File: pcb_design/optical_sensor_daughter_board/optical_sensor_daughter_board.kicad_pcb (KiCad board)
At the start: 2 copper layers, 22.9 x 44.5 mm, 2 parts, among them J1 Conn_02x06_Counter_Clockwise, U1 PMW3389

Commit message: WIP daughter board
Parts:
- added C1: 0.1uF, Capacitor_SMD:C_0603_1608Metric_Pad1.05x0.95mm_HandSolder, F.Cu at (137.7, 85.2)
- added C2: 4.7uF, Capacitor_SMD:C_0603_1608Metric_Pad1.05x0.95mm_HandSolder, F.Cu at (139.6, 85.2)
- added C3: 1uF, Capacitor_SMD:C_0603_1608Metric_Pad1.05x0.95mm_HandSolder, F.Cu at (144.3, 110.0)
- added C4: 1uF, Capacitor_SMD:C_0603_1608Metric_Pad1.05x0.95mm_HandSolder, F.Cu at (130.4, 109.2)
- added R1: 10K, Resistor_SMD:R_0603_1608Metric_Pad1.05x0.95mm_HandSolder, F.Cu at (141.3, 85.2)
- added R2: 39, Resistor_SMD:R_0603_1608Metric_Pad1.05x0.95mm_HandSolder, F.Cu at (126.7, 109.2)
- added U2: PMW3360, pmw3389:PMW3389, F.Cu at (135.6, 96.8)
- added U3: SN74LVC1T45DBV, Package_TO_SOT_SMD:SOT-23-6, F.Cu at (126.6, 87.2)
- added U4: SN74LVC1T45DBV, Package_TO_SOT_SMD:SOT-23-6, F.Cu at (126.5, 94.8)
- added U5: SN74LVC1T45DBV, Package_TO_SOT_SMD:SOT-23-6, F.Cu at (126.5, 98.7)
- added U6: SN74LVC1T45DBV, Package_TO_SOT_SMD:SOT-23-6, F.Cu at (126.5, 102.5)
- added U7: SN74LVC1T45DBV, Package_TO_SOT_SMD:SOT-23-6, F.Cu at (126.6, 91.0)
- J1: value Conn_02x06_Counter_Clockwise -> Conn_01x08_Male; footprint Connector_PinHeader_2.54mm:PinHeader_2x06_P2.54mm_Vertical -> Connector_PinHeader_2.54mm:PinHeader_1x08_P2.54mm_Vertical
- U1: value PMW3389 -> TLV70019_SOT23-5; footprint pmw3389:PMW3389 -> Package_TO_SOT_SMD:SOT-23-5
- moved J1 13.7 mm to (143.9, 106.0)
- moved U1 9.62 mm to (140.3, 109.2)
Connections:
- J1 pad 1: GND -> VIN
- J1 pad 2: MOTION -> MISO_3.3V
- J1 pad 3: NRESET -> MOIS_3.3V
- J1 pad 4: SCLK -> SLCK_3.3V
- J1 pad 5: GPO -> SS_3.3V
- J1 pad 6: MOSI -> MOTION_3.3V
- J1 pad 7: VDDIO -> GND
- J1 pad 8: MISO -> RESET
- U1 pad 1: (no net) -> VIN
- U1 pad 2: (no net) -> Net-(C3-Pad2)
- U1 pad 3: VDCPIX -> VIN
- U1 pad 4: VDD -> (no net)
- U1 pad 5: VDDIO -> VDD
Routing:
- net VDD: track 27.5 -> 97.6 mm, vias 0 -> 4
- net VIN: track 0.00 -> 65.4 mm
- net GND: track 9.00 -> 62.9 mm
- net SLCK_3.3V: track 0.00 -> 45.3 mm, vias 0 -> 2
- net MISO_3.3V: track 0.00 -> 37.0 mm, vias 0 -> 1
- net SS_3.3V: track 0.00 -> 36.1 mm, vias 0 -> 3
- net MOIS_3.3V: track 0.00 -> 33.0 mm, vias 0 -> 1
- net LED_P: track 33.0 -> 0.00 mm
- net VDCPIX: track 32.7 -> 0.00 mm
- net MOTION_3.3V: track 0.00 -> 28.2 mm, vias 0 -> 1
- net NCS: track 26.5 -> 0.00 mm
- net Net-(C3-Pad2): track 0.00 -> 23.4 mm
- net VDDIO: track 22.8 -> 0.00 mm
- net GPO: track 18.1 -> 0.00 mm
- net Net-(C1-Pad2): track 0.00 -> 17.9 mm
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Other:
- board size 22.9 x 44.5 mm -> 23 x 28 mm

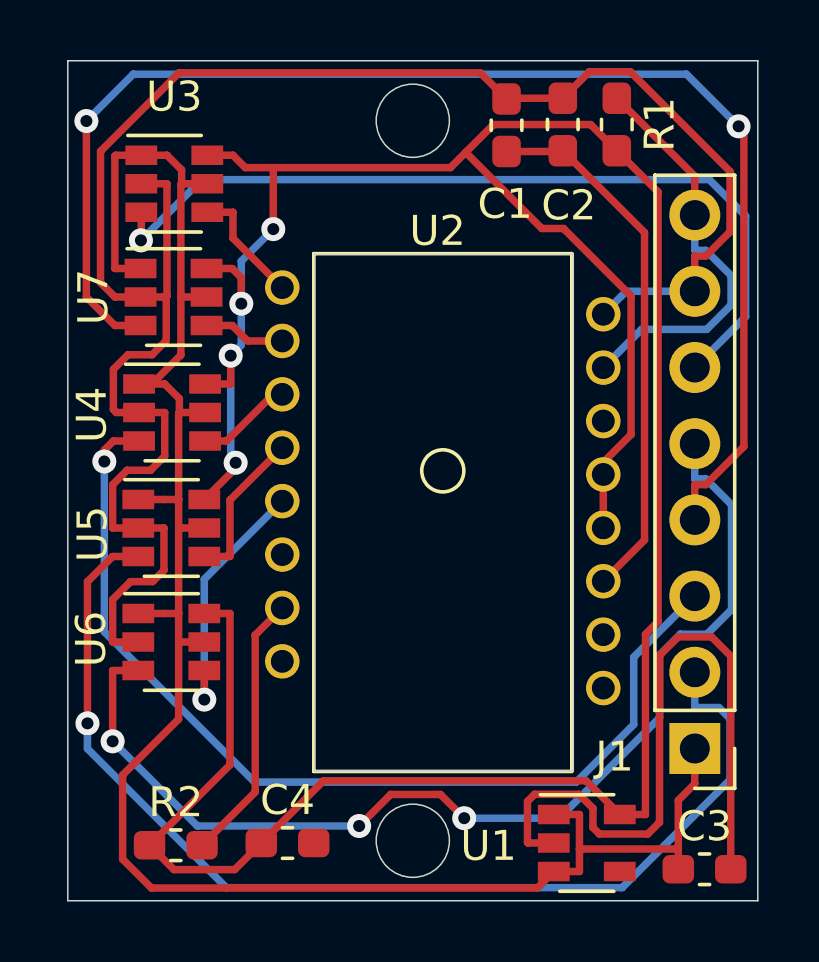
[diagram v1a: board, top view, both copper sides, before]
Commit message: New 0x08 firmware added
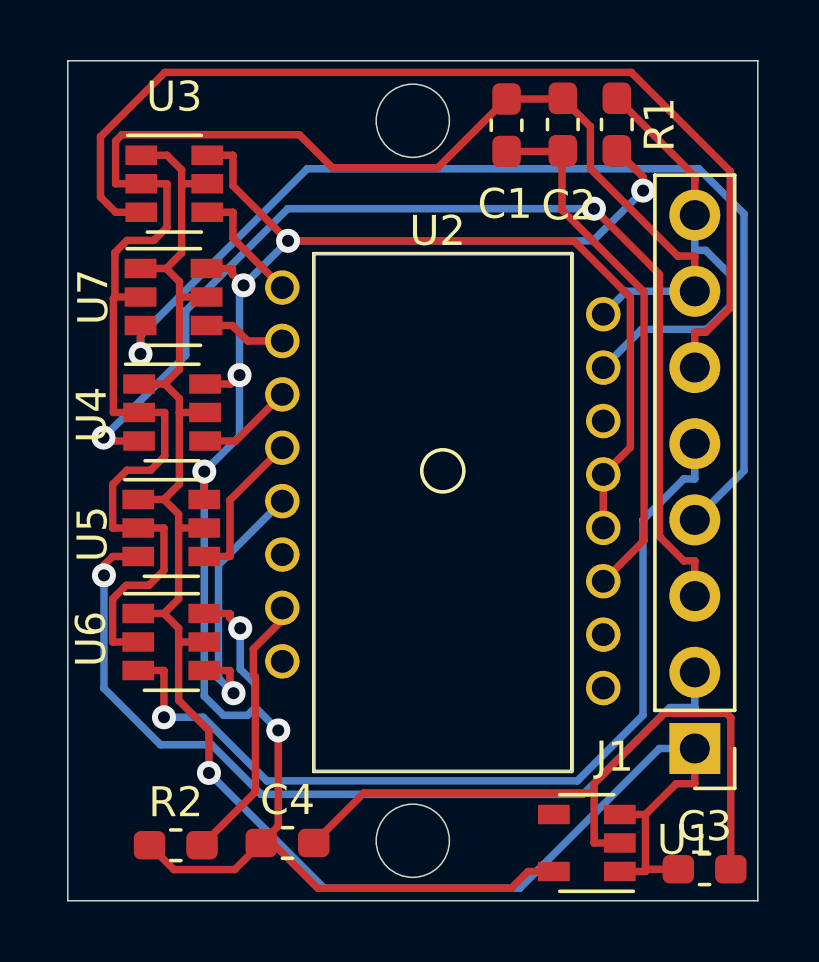
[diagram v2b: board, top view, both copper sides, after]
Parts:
- turned U1 to 180 degrees
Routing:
- net VDD: track 97.6 -> 85.5 mm, vias 4 -> 7
- net SLCK_3.3V: track 45.3 -> 35.5 mm, vias 2 -> 1
- net MISO_3.3V: track 37.0 -> 28.9 mm
- net GND: track 62.9 -> 55.5 mm
- net VIN: track 65.4 -> 59.1 mm, vias 0 -> 1
- net SS_3.3V: track 36.1 -> 30.1 mm, vias 3 -> 1
- net MOTION_3.3V: track 28.2 -> 34.1 mm, vias 1 -> 0
- net MOIS_3.3V: track 33.0 -> 36.1 mm, vias 1 -> 2
